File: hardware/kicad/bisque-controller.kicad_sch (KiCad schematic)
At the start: 0 parts

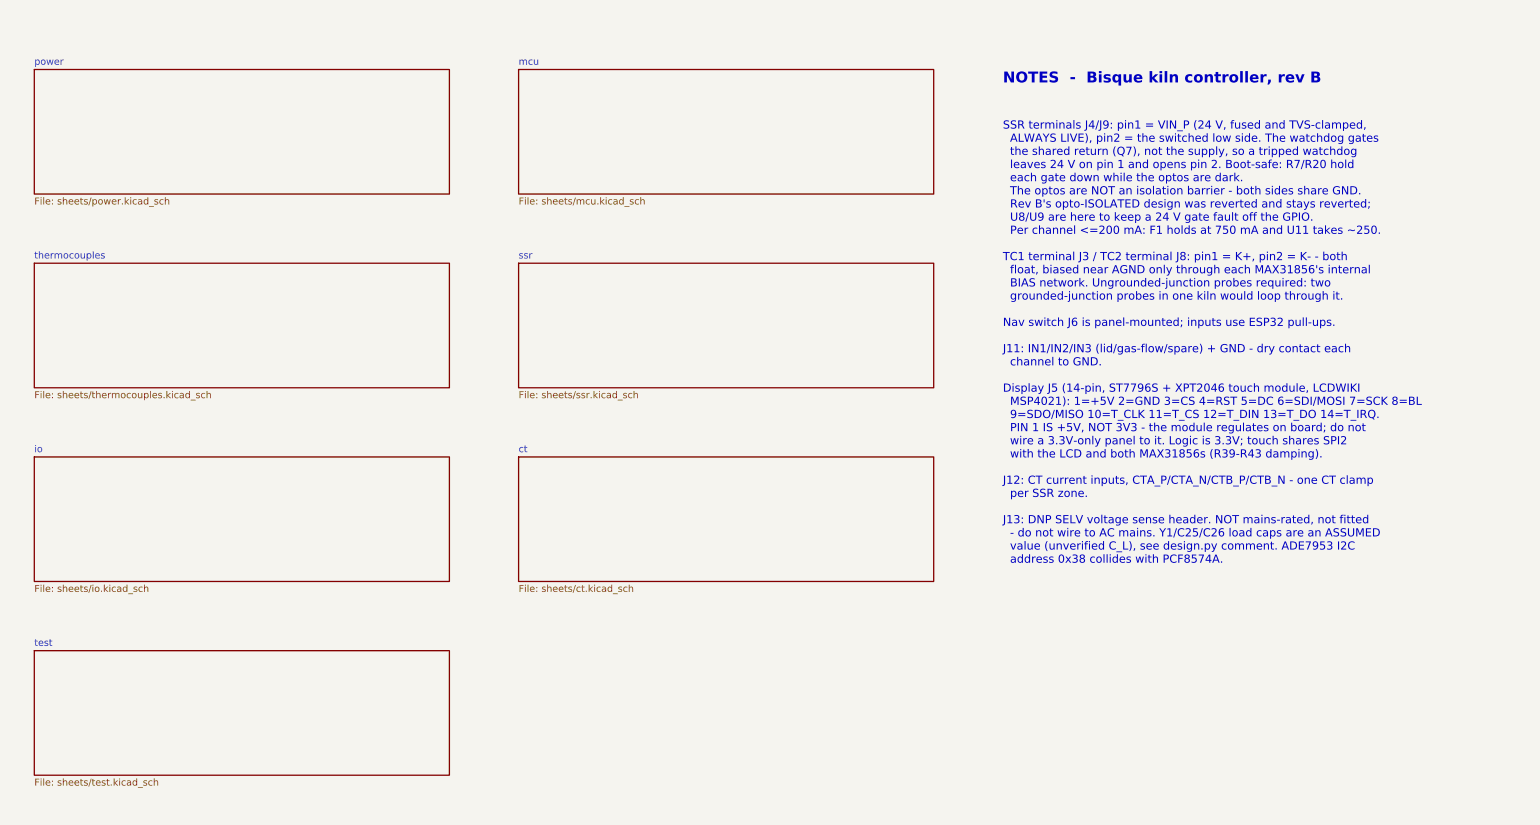
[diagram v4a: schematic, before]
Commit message: hardware: hierarchical schematic, ERC at 0/0, rev B.3
Applies items 1-3 of SCHEMATIC-REVIEW-2026-10-22.md.

ERC: the 173 lib_symbol_mismatch warnings were over-escaped quotes in the
embedded power symbols' Description strings; refreshed from the library.
The 18 off-grid power symbols are snapped and their stub wires redrawn.
The VIN and VLED global labels that existed only to carry a PWR_FLAG are
gone; the flags now sit on the nets they drive (J2.1, the VLED junction).
ERC reads 0 errors / 0 warnings with the documented SDO exclusion.

Hierarchy: no global labels remain. Each net that crosses sheets has one
hierarchical label per sheet, matching sheet pins on the root, and the
root wires those pins as a block diagram. Every other former global label
is a local label. The eight signal test points (TP4-TP11) move from the
test sheet to the mcu and ct sheets beside their nets, so the test block
needs no pins. KiCad names the nets /mcu/SPI_MISO etc.; netlist.py strips
the path, so the board's net names and the routing tables are unchanged
(182 components, 538 pads, 0 mismatches). single_global_label is now a
warning. check_sync_idempotent's collision fixture used the bare
"SPI_MISO" name and is updated, with a loud failure if its victims vanish.

Drawing: rev B.3 dated 2026-10-22 on every sheet, ct on A3 like the rest,
the three overflowing titles shortened, and the notes no longer refer to
design.py or to crystal load caps that no longer exist.

Co-Authored-By: Claude Fable 5.1 <noreply@anthropic.com>
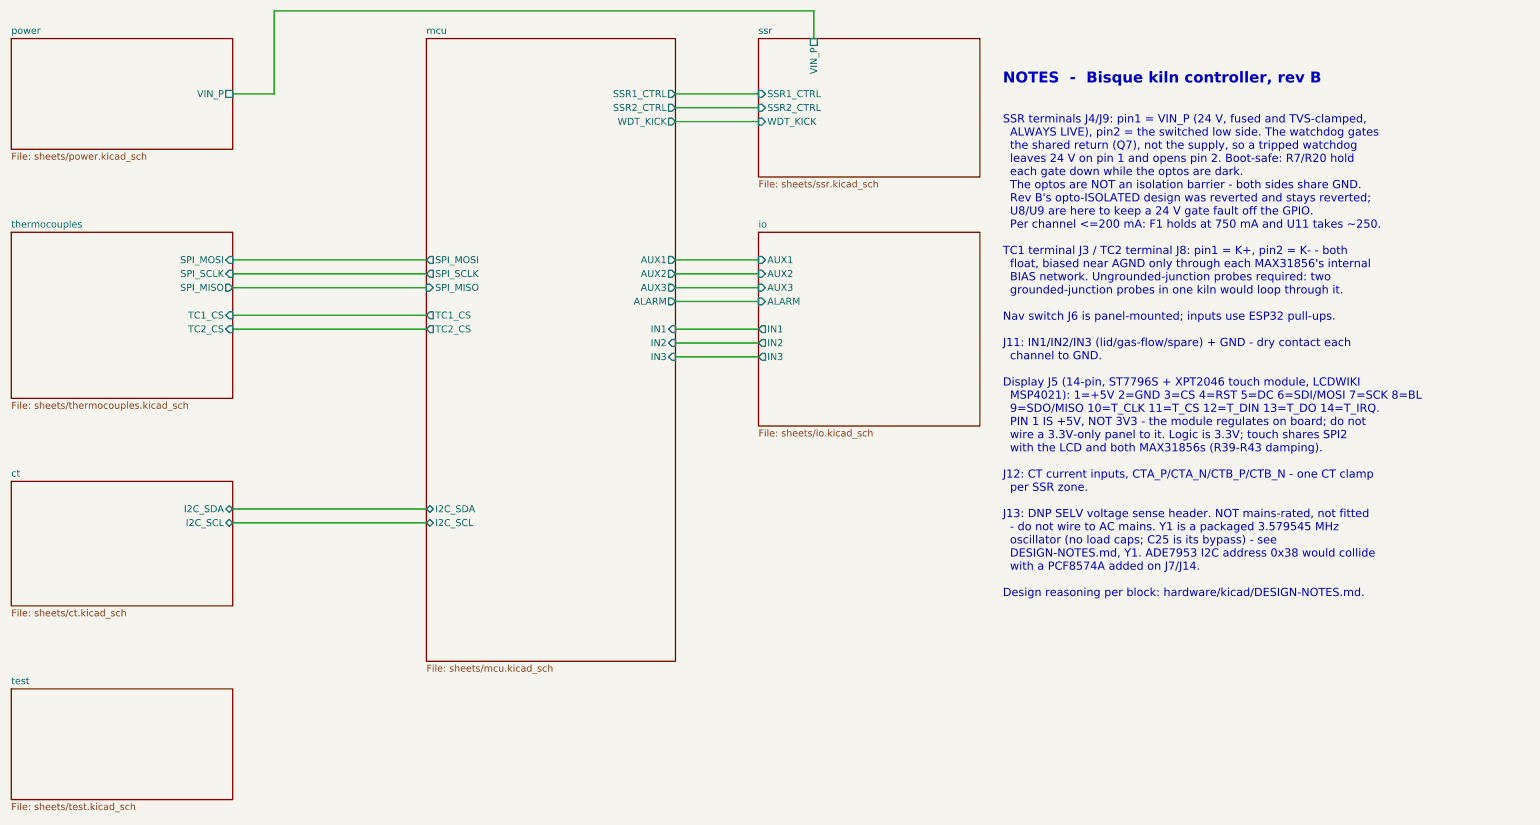
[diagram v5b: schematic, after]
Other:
- sheet ct ports: added I2C_SCL, I2C_SDA; removed none
- sheet io ports: added ALARM, AUX1, AUX2, AUX3, IN1, IN2, IN3; removed none
- sheet mcu ports: added ALARM, AUX1, AUX2, AUX3, I2C_SCL, I2C_SDA, IN1, IN2, IN3, SPI_MISO, SPI_MOSI, SPI_SCLK, SSR1_CTRL, SSR2_CTRL, TC1_CS, TC2_CS, WDT_KICK; removed none
- sheet power ports: added VIN_P; removed none
- sheet ssr ports: added SSR1_CTRL, SSR2_CTRL, VIN_P, WDT_KICK; removed none
- sheet thermocouples ports: added SPI_MISO, SPI_MOSI, SPI_SCLK, TC1_CS, TC2_CS; removed none

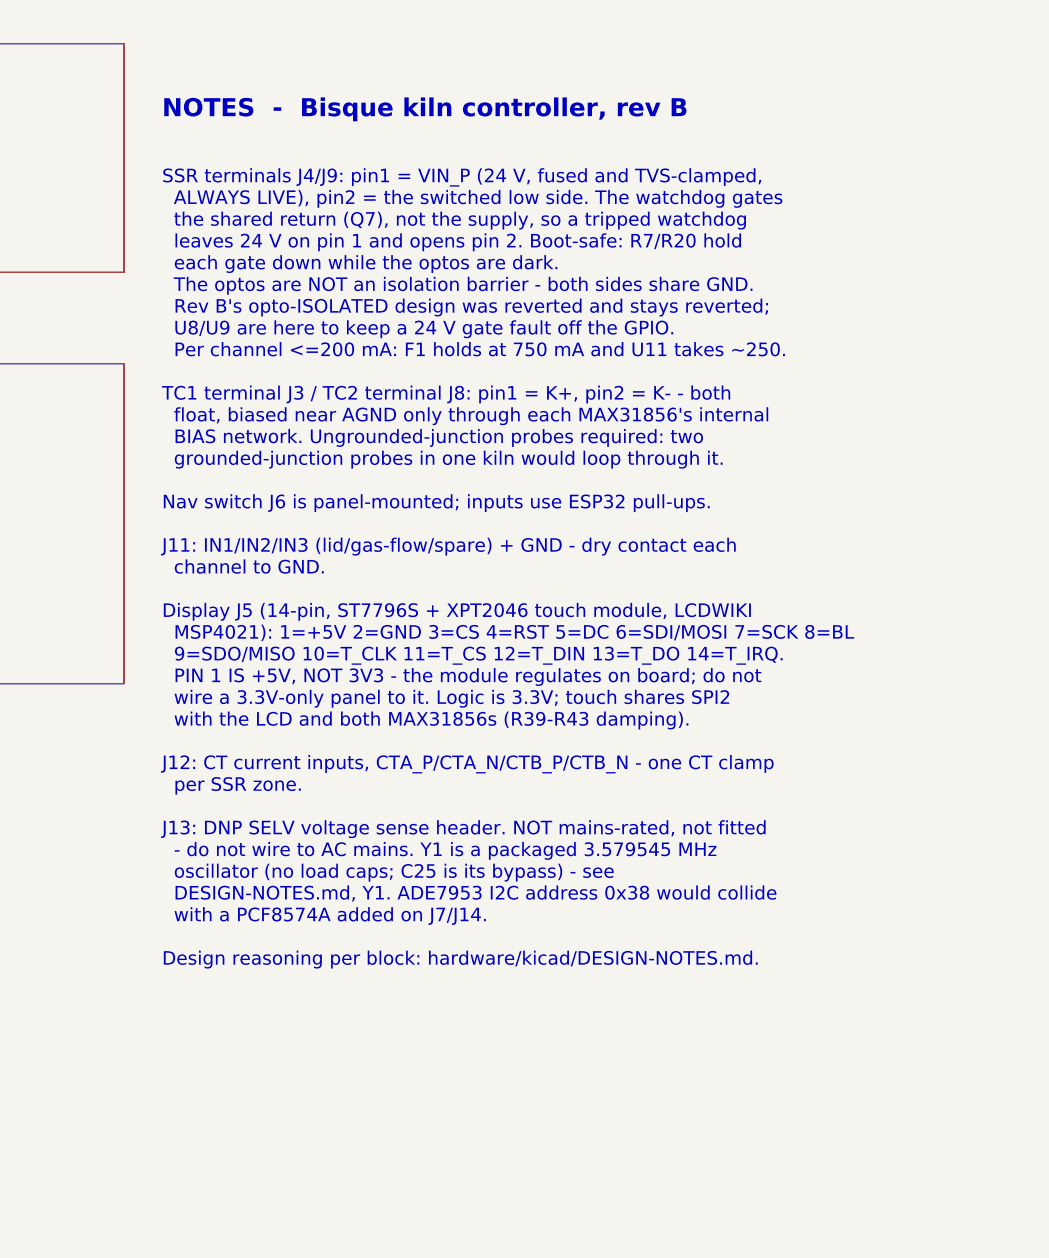
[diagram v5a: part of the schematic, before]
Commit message: hardware: honest symbols, real MPNs, U6 spares grounded, LCD_RST verified
Third batch from SCHEMATIC-REVIEW-2026-10-22.md (findings 6, 8, 11, 17,
18 and E1/E2).

Symbols: D8 is bisque:SMAJ30A (drawn as a zener with its cathode on the
rail, since the fitted TVS is unidirectional), Q5-Q7 are bisque:CJ2310
and U2 is bisque:TLV1117LV33, each a flattened copy of the stock symbol
with the fitted part's name, description and LCSC-hosted datasheet, so
no pin or wire moved. The stock D_TVS, 2N7002 and TLV1117-33 embeds are
gone from the sheets.

Sourcing: every one of the 160 assembled symbols now carries MPN (the
manufacturer's part number, from LCSC's product record for its C-number),
Manufacturer and Datasheet (LCSC's hosted PDF) beside LCSC. check_mpn.py
keeps LCSC tied to gen_jlc.LCSC and requires the other two to be present
and MPN not to be a bare C-number.

Drawing: J11's IN1_RAW/IN2_RAW labels read along their own wires instead
of across the connector; U6's unused Darlington inputs I4-I7 are tied to
GND (the board's F.Cu pour already covers them - 4 pads re-netted, 0
unconnected, DRC 0); the root notes record the retired designators and
the LCD_RST finding (the MSP4021's own schematic shows no pull-up on
RESET, so GPIO46 does not block download mode); the mcu sheet notes that
GPIO35/36 rule out R8 (octal PSRAM) modules.

The datasheet manifest maps the shared 22uF/25V sheet to the unified
value and exempts the test points' net-name values. Full make pcb-check
passes; gerbers differ by timestamp and the re-filled GND pour; 3D
renders refreshed.

Co-Authored-By: Claude Fable 5.1 <noreply@anthropic.com>
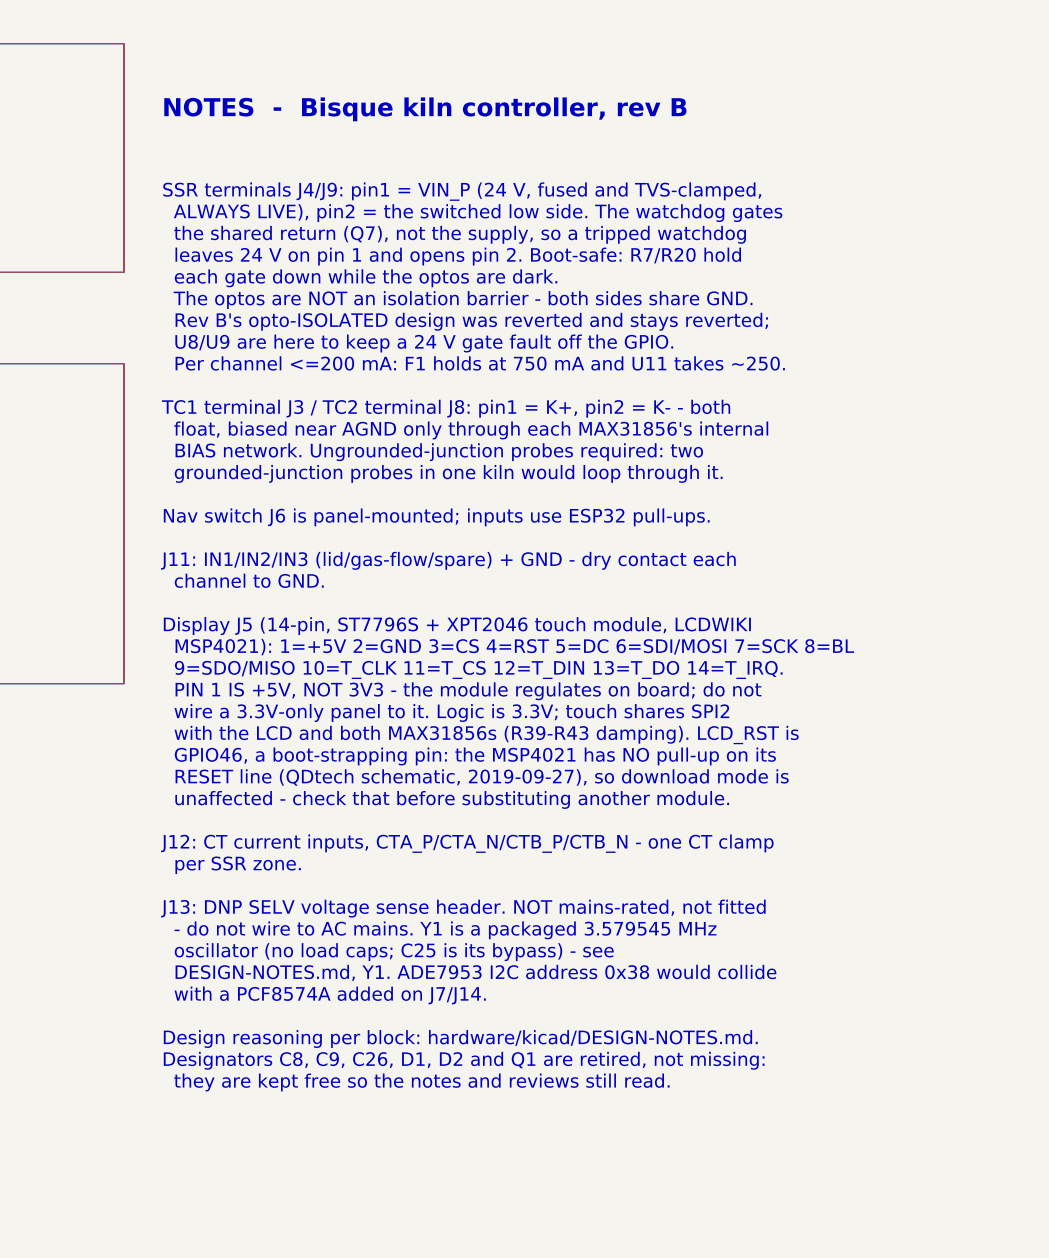
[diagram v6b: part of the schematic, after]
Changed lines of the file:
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@@
 		)
 	)
-	(text "SSR terminals J4/J9: pin1 = VIN_P (24 V, fused and TVS-clamped,\n  ALWAYS LIVE), pin2 = the switched low side. The watchdog gates\n  the shared return (Q7), not the supply, so a tripped watchdog\n  leaves 24 V on pin 1 and opens pin 2. Boot-safe: R7/R20 hold\n  each gate down while the optos are dark.\n  The optos are NOT an isolation barrier - both sides share GND.\n  Rev B's opto-ISOLATED design was reverted and stays reverted;\n  U8/U9 are here to keep a 24 V gate fault off the GPIO.\n  Per channel <=200 mA: F1 holds at 750 mA and U11 takes ~250.\n\nTC1 terminal J3 / TC2 terminal J8: pin1 = K+, pin2 = K- - both\n  float, biased near AGND only through each MAX31856's internal\n  BIAS network. Ungrounded-junction probes required: two\n  grounded-junction probes in one kiln would loop through it.\n\nNav switch J6 is panel-mounted; inputs use ESP32 pull-ups.\n\nJ11: IN1/IN2/IN3 (lid/gas-flow/spare) + GND - dry contact each\n  channel to GND.\n\nDisplay J5 (14-pin, ST7796S + XPT2046 touch module, LCDWIKI\n  MSP4021): 1=+5V 2=GND 3=CS 4=RST 5=DC 6=SDI/MOSI 7=SCK 8=BL\n  9=SDO/MISO 10=T_CLK 11=T_CS 12=T_DIN 13=T_DO 14=T_IRQ.\n  PIN 1 IS +5V, NOT 3V3 - the module regulates on board; do not\n  wire a 3.3V-only panel to it. Logic is 3.3V; touch shares SPI2\n  with the LCD and both MAX31856s (R39-R43 damping).\n\nJ12: CT current inputs, CTA_P/CTA_N/CTB_P/CTB_N - one CT clamp\n  per SSR zone.\n\nJ13: DNP SELV voltage sense header. NOT mains-rated, not fitted\n  - do not wire to AC mains. Y1 is a packaged 3.579545 MHz\n  oscillator (no load caps; C25 is its bypass) - see\n  DESIGN-NOTES.md, Y1. ADE7953 I2C address 0x38 would collide\n  with a PCF8574A added on J7/J14.\n\nDesign reasoning per block: hardware/kicad/DESIGN-NOTES.md."
+	(text "SSR terminals J4/J9: pin1 = VIN_P (24 V, fused and TVS-clamped,\n  ALWAYS LIVE), pin2 = the switched low side. The watchdog gates\n  the shared return (Q7), not the supply, so a tripped watchdog\n  leaves 24 V on pin 1 and opens pin 2. Boot-safe: R7/R20 hold\n  each gate down while the optos are dark.\n  The optos are NOT an isolation barrier - both sides share GND.\n  Rev B's opto-ISOLATED design was reverted and stays reverted;\n  U8/U9 are here to keep a 24 V gate fault off the GPIO.\n  Per channel <=200 mA: F1 holds at 750 mA and U11 takes ~250.\n\nTC1 terminal J3 / TC2 terminal J8: pin1 = K+, pin2 = K- - both\n  float, biased near AGND only through each MAX31856's internal\n  BIAS network. Ungrounded-junction probes required: two\n  grounded-junction probes in one kiln would loop through it.\n\nNav switch J6 is panel-mounted; inputs use ESP32 pull-ups.\n\nJ11: IN1/IN2/IN3 (lid/gas-flow/spare) + GND - dry contact each\n  channel to GND.\n\nDisplay J5 (14-pin, ST7796S + XPT2046 touch module, LCDWIKI\n  MSP4021): 1=+5V 2=GND 3=CS 4=RST 5=DC 6=SDI/MOSI 7=SCK 8=BL\n  9=SDO/MISO 10=T_CLK 11=T_CS 12=T_DIN 13=T_DO 14=T_IRQ.\n  PIN 1 IS +5V, NOT 3V3 - the module regulates on board; do not\n  wire a 3.3V-only panel to it. Logic is 3.3V; touch shares SPI2\n  with the LCD and both MAX31856s (R39-R43 damping). LCD_RST is\n  GPIO46, a boot-strapping pin: the MSP4021 has NO pull-up on its\n  RESET line (QDtech schematic, 2019-09-27), so download mode is\n  unaffected - check that before substituting another module.\n\nJ12: CT current inputs, CTA_P/CTA_N/CTB_P/CTB_N - one CT clamp\n  per SSR zone.\n\nJ13: DNP SELV voltage sense header. NOT mains-rated, not fitted\n  - do not wire to AC mains. Y1 is a packaged 3.579545 MHz\n  oscillator (no load caps; C25 is its bypass) - see\n  DESIGN-NOTES.md, Y1. ADE7953 I2C address 0x38 would collide\n  with a PCF8574A added on J7/J14.\n\nDesign reasoning per block: hardware/kicad/DESIGN-NOTES.md.\nDesignators C8, C9, C26, D1, D2 and Q1 are retired, not missing:\n  they are kept free so the notes and reviews still read."
 		(exclude_from_sim no)
-		(at 199.8 78.74 0)
+		(at 199.8 86.36 0)
 		(effects
 			(font
